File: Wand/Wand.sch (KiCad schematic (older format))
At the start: 20 parts, among them IC1 ATMEGA328P-A, J1 TIP, P1 ISP, P2 BASE, U1 OPA336U, U2 MPU-6050, Y1 16MHz

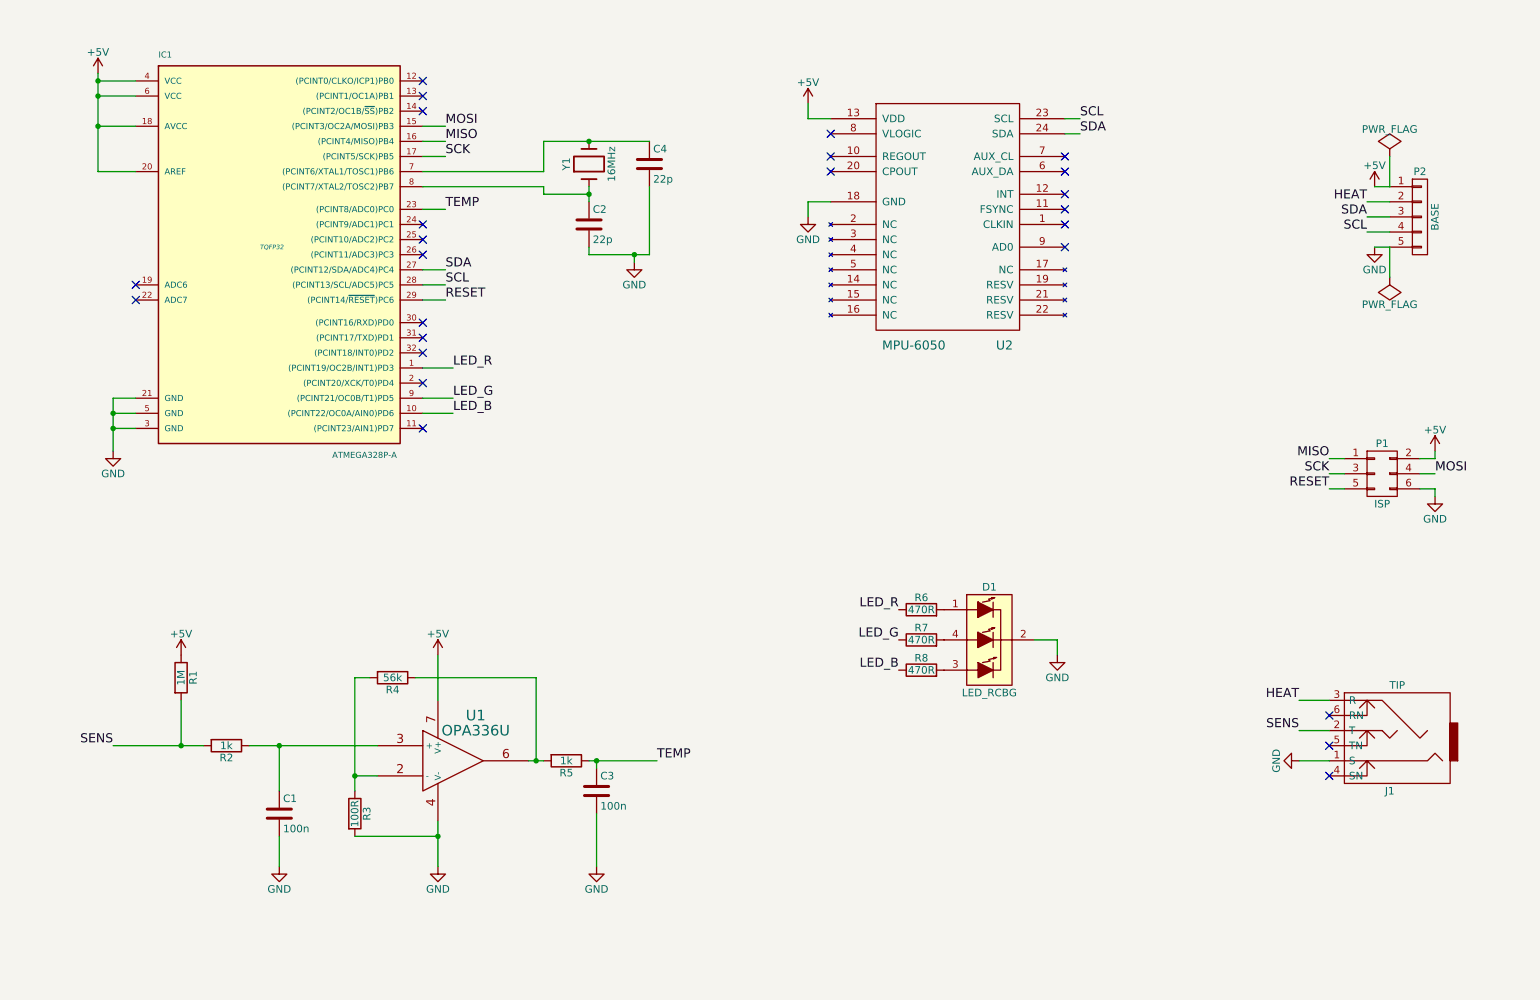
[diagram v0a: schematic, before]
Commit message: Changed logic voltage to 3.3V as the MCP-6050 is 3,3v (as are most accelerometers)
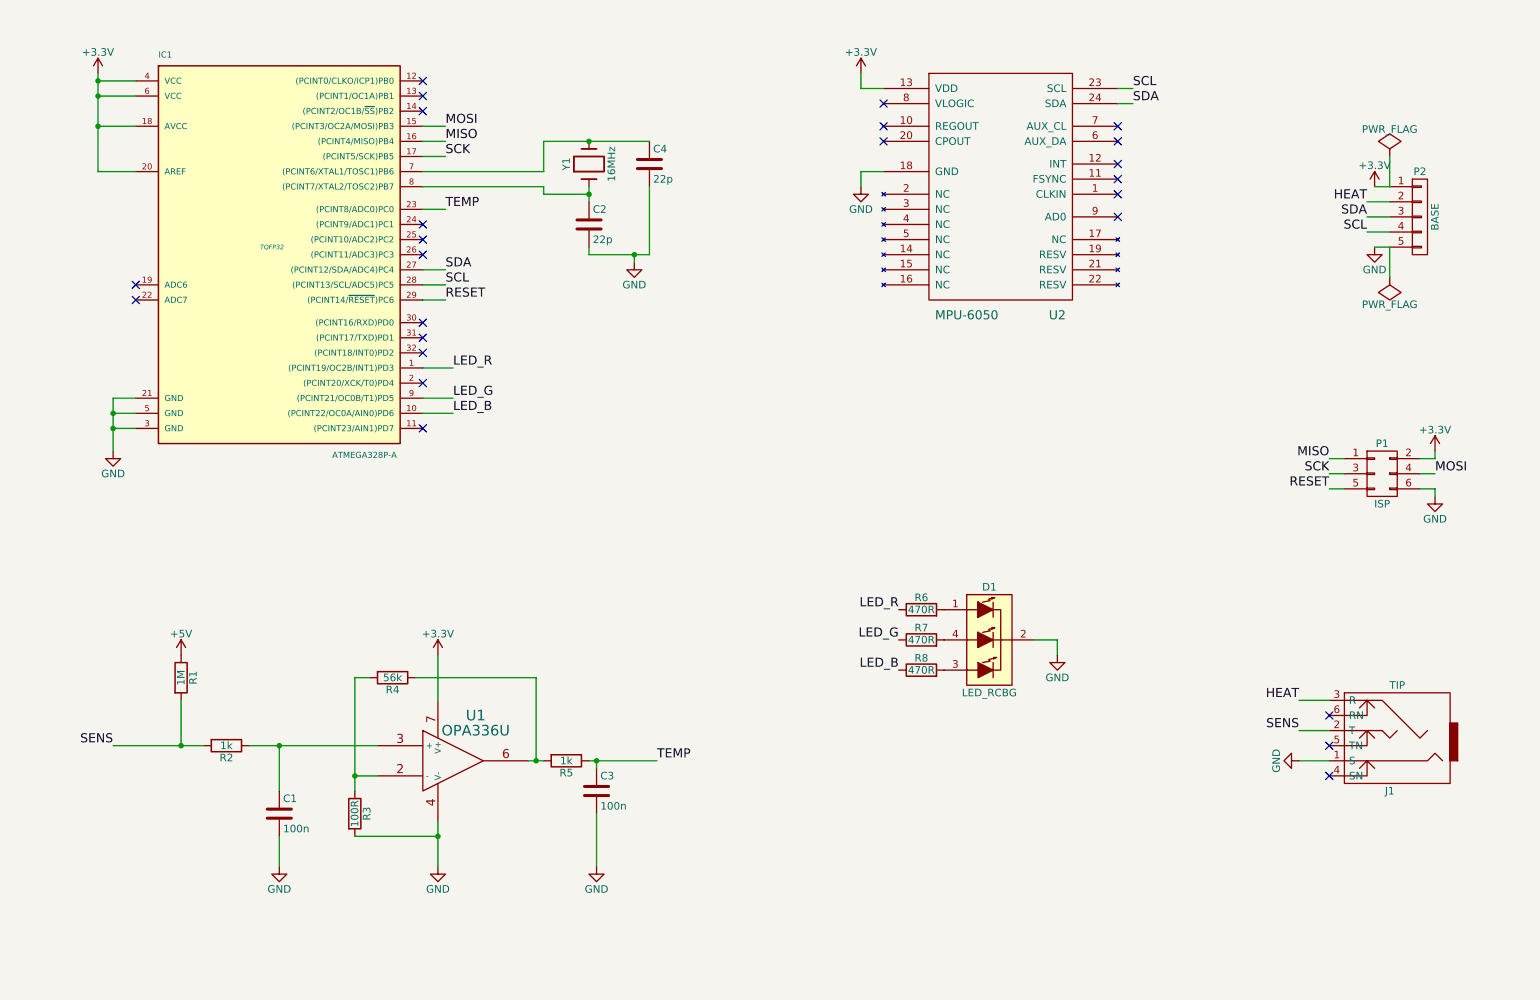
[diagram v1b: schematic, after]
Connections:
- net +5V: no longer IC1.18 (AVCC), IC1.20 (AREF), IC1.4 (VCC), IC1.6 (VCC), P1.2 (P2), P2.1 (P1), U1.7 (V+), U2.13 (VDD)
- new net +3V3: IC1.18 (AVCC), IC1.20 (AREF), IC1.4 (VCC), IC1.6 (VCC), P1.2 (P2), P2.1 (P1), U1.7 (V+), U2.13 (VDD)
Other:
- moved on the sheet: U2
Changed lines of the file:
@@
 LIBS:valves
 LIBS:mpu-6050
+LIBS:Wand
 LIBS:Wand-cache
 EELAYER 25 0
@@
 L MPU-6050 U2
 U 1 1 56411594
-P 7100 2300
-F 0 "U2" H 7450 1600 60  0000 C CNN
-F 1 "MPU-6050" H 6850 1600 60  0000 C CNN
-F 2 "" H 7100 2050 60  0000 C CNN
-F 3 "" H 7100 2050 60  0000 C CNN
-	1    7100 2300
+P 7450 2100
+F 0 "U2" H 7800 1400 60  0000 C CNN
+F 1 "MPU-6050" H 7200 1400 60  0000 C CNN
+F 2 "" H 7450 1850 60  0000 C CNN
+F 3 "" H 7450 1850 60  0000 C CNN
+	1    7450 2100
 	1    0    0    -1
 $EndComp
@@
 $EndComp
 $Comp
-L +5V #PWR01
-U 1 1 564124F5
-P 3700 5050
-F 0 "#PWR01" H 3700 4900 50  0001 C CNN
-F 1 "+5V" H 3700 5190 50  0000 C CNN
-F 2 "" H 3700 5050 60  0000 C CNN
-F 3 "" H 3700 5050 60  0000 C CNN
-	1    3700 5050
-	1    0    0    -1
-$EndComp
-$Comp
 L GND #PWR02
 U 1 1 5641252D
@@
 F 3 "" H 5000 2450 60  0000 C CNN
 	1    5000 2450
-	1    0    0    -1
-$EndComp
-$Comp
-L +5V #PWR08
-U 1 1 56415353
-P 1450 1200
-F 0 "#PWR08" H 1450 1050 50  0001 C CNN
-F 1 "+5V" H 1450 1340 50  0000 C CNN
-F 2 "" H 1450 1200 60  0000 C CNN
-F 3 "" H 1450 1200 60  0000 C CNN
-	1    1450 1200
 	1    0    0    -1
 $EndComp
@@
 Text Label 9600 3950 2    60   ~ 0
 RESET
-$Comp
-L +5V #PWR011
-U 1 1 56417CD8
-P 10300 3700
-F 0 "#PWR011" H 10300 3550 50  0001 C CNN
-F 1 "+5V" H 10300 3840 50  0000 C CNN
-F 2 "" H 10300 3700 60  0000 C CNN
-F 3 "" H 10300 3700 60  0000 C CNN
-	1    10300 3700
-	1    0    0    -1
-$EndComp
 Text Label 10300 3850 0    60   ~ 0
 MOSI
@@
 	1    0    0    -1
 $EndComp
-$Comp
-L +5V #PWR014
-U 1 1 56418042
-P 9900 1950
-F 0 "#PWR014" H 9900 1800 50  0001 C CNN
-F 1 "+5V" H 9900 2090 50  0000 C CNN
-F 2 "" H 9900 1950 60  0000 C CNN
-F 3 "" H 9900 1950 60  0000 C CNN
-	1    9900 1950
-	1    0    0    -1
-$EndComp
 Text Label 9850 2050 2    60   ~ 0
 HEAT
@@
 SCL
 Wire Wire Line
-	1550 5650 2150 5650
+	1550 5650 2000 5650
+Wire Wire Line
+	2000 5650 2150 5650
 Wire Wire Line
 	2000 5350 2000 5650
 Connection ~ 2000 5650
 Wire Wire Line
-	2450 5650 3300 5650
+	2450 5650 2650 5650
+Wire Wire Line
+	2650 5650 3300 5650
 Wire Wire Line
 	2650 5950 2650 5650
@@
 	2650 6250 2650 6450
 Wire Wire Line
-	3150 5200 3150 5950
+	3150 5200 3150 5850
+Wire Wire Line
+	3150 5850 3150 5950
 Wire Wire Line
 	3150 5850 3300 5850
@@
 	4350 5200 4350 5750
 Wire Wire Line
-	4300 5750 4400 5750
+	4300 5750 4350 5750
+Wire Wire Line
+	4350 5750 4400 5750
 Connection ~ 4350 5750
 Wire Wire Line
@@
 	3150 6250 3700 6250
 Wire Wire Line
-	3700 6150 3700 6450
+	3700 6150 3700 6250
+Wire Wire Line
+	3700 6250 3700 6450
 Connection ~ 3700 6250
 Wire Wire Line
 	4750 6100 4750 6450
 Wire Wire Line
-	4700 5750 5150 5750
+	4700 5750 4750 5750
+Wire Wire Line
+	4750 5750 5150 5750
 Wire Wire Line
 	4750 5750 4750 5800
@@
 	4400 1850 4400 1650
 Wire Wire Line
-	4400 1650 5100 1650
-Wire Wire Line
-	4700 1950 4700 2050
+	4400 1650 4700 1650
+Wire Wire Line
+	4700 1650 5100 1650
+Wire Wire Line
+	4700 1950 4700 2000
+Wire Wire Line
+	4700 2000 4700 2050
 Connection ~ 4700 1650
 Wire Wire Line
@@
 	5100 2400 5100 1950
 Wire Wire Line
-	4700 2400 5100 2400
+	4700 2400 5000 2400
+Wire Wire Line
+	5000 2400 5100 2400
 Wire Wire Line
 	5000 2400 5000 2450
@@
 Connection ~ 5000 2400
 Wire Wire Line
-	1450 1200 1450 1850
+	1450 1200 1450 1250
+Wire Wire Line
+	1450 1250 1450 1350
+Wire Wire Line
+	1450 1350 1450 1550
+Wire Wire Line
+	1450 1550 1450 1850
 Wire Wire Line
 	1450 1250 1700 1250
@@
 Connection ~ 1450 1250
 Wire Wire Line
-	1550 3350 1550 3700
+	1550 3350 1550 3450
+Wire Wire Line
+	1550 3450 1550 3550
+Wire Wire Line
+	1550 3550 1550 3700
 Wire Wire Line
 	1550 3550 1700 3550
@@
 Wire Wire Line
 	9900 2350 10000 2350
-Text Label 7950 1600 0    60   ~ 0
+Text Label 8300 1400 0    60   ~ 0
 SDA
-Text Label 7950 1500 0    60   ~ 0
+Text Label 8300 1300 0    60   ~ 0
 SCL
 Wire Wire Line
-	7950 1500 7850 1500
-Wire Wire Line
-	7850 1600 7950 1600
-$Comp
-L +5V #PWR015
-U 1 1 56419539
-P 6150 1400
-F 0 "#PWR015" H 6150 1250 50  0001 C CNN
-F 1 "+5V" H 6150 1540 50  0000 C CNN
-F 2 "" H 6150 1400 60  0000 C CNN
-F 3 "" H 6150 1400 60  0000 C CNN
-	1    6150 1400
-	1    0    0    -1
-$EndComp
+	8300 1300 8200 1300
+Wire Wire Line
+	8200 1400 8300 1400
 $Comp
 L GND #PWR016
 U 1 1 56419575
-P 6150 2150
-F 0 "#PWR016" H 6150 1900 50  0001 C CNN
-F 1 "GND" H 6150 2000 50  0000 C CNN
-F 2 "" H 6150 2150 60  0000 C CNN
-F 3 "" H 6150 2150 60  0000 C CNN
-	1    6150 2150
-	1    0    0    -1
-$EndComp
-Wire Wire Line
-	6150 2050 6150 2150
-Wire Wire Line
-	6150 2050 6300 2050
-Wire Wire Line
-	6300 1500 6150 1500
-Wire Wire Line
-	6150 1500 6150 1400
+P 6500 1950
+F 0 "#PWR016" H 6500 1700 50  0001 C CNN
+F 1 "GND" H 6500 1800 50  0000 C CNN
+F 2 "" H 6500 1950 60  0000 C CNN
+F 3 "" H 6500 1950 60  0000 C CNN
+	1    6500 1950
+	1    0    0    -1
+$EndComp
+Wire Wire Line
+	6500 1850 6500 1950
+Wire Wire Line
+	6500 1850 6650 1850
+Wire Wire Line
+	6650 1300 6500 1300
+Wire Wire Line
+	6500 1300 6500 1200
 Text Label 3750 2500 0    60   ~ 0
 SDA
@@
 NoConn ~ 3600 1350
 NoConn ~ 3600 1250
-NoConn ~ 6300 1600
-NoConn ~ 6300 1750
-NoConn ~ 6300 1850
-NoConn ~ 7850 2350
-NoConn ~ 7850 2200
-NoConn ~ 7850 2100
-NoConn ~ 7850 2000
-NoConn ~ 7850 1850
-NoConn ~ 7850 1750
+NoConn ~ 6650 1400
+NoConn ~ 6650 1550
+NoConn ~ 6650 1650
+NoConn ~ 8200 2150
+NoConn ~ 8200 2000
+NoConn ~ 8200 1900
+NoConn ~ 8200 1800
+NoConn ~ 8200 1650
+NoConn ~ 8200 1550
 $Comp
 L PWR_FLAG #FLG017
@@
 Wire Wire Line
 	10300 3950 10300 4000
+$Comp
+L +3.3V #PWR?
+U 1 1 5647AD9A
+P 9900 1950
+F 0 "#PWR?" H 9900 1800 50  0001 C CNN
+F 1 "+3.3V" H 9900 2090 50  0000 C CNN
+F 2 "" H 9900 1950 60  0000 C CNN
+F 3 "" H 9900 1950 60  0000 C CNN
+	1    9900 1950
+	1    0    0    -1
+$EndComp
+$Comp
+L +3.3V #PWR?
+U 1 1 5647B486
+P 6500 1200
+F 0 "#PWR?" H 6500 1050 50  0001 C CNN
+F 1 "+3.3V" H 6500 1340 50  0000 C CNN
+F 2 "" H 6500 1200 60  0000 C CNN
+F 3 "" H 6500 1200 60  0000 C CNN
+	1    6500 1200
+	1    0    0    -1
+$EndComp
+$Comp
+L +3.3V #PWR?
+U 1 1 5647BAD5
+P 1450 1200
+F 0 "#PWR?" H 1450 1050 50  0001 C CNN
+F 1 "+3.3V" H 1450 1340 50  0000 C CNN
+F 2 "" H 1450 1200 60  0000 C CNN
+F 3 "" H 1450 1200 60  0000 C CNN
+	1    1450 1200
+	1    0    0    -1
+$EndComp
+$Comp
+L +3.3V #PWR?
+U 1 1 5647C7BA
+P 3700 5050
+F 0 "#PWR?" H 3700 4900 50  0001 C CNN
+F 1 "+3.3V" H 3700 5190 50  0000 C CNN
+F 2 "" H 3700 5050 60  0000 C CNN
+F 3 "" H 3700 5050 60  0000 C CNN
+	1    3700 5050
+	1    0    0    -1
+$EndComp
+$Comp
+L +3.3V #PWR?
+U 1 1 5647DBFE
+P 10300 3700
+F 0 "#PWR?" H 10300 3550 50  0001 C CNN
+F 1 "+3.3V" H 10300 3840 50  0000 C CNN
+F 2 "" H 10300 3700 60  0000 C CNN
+F 3 "" H 10300 3700 60  0000 C CNN
+	1    10300 3700
+	1    0    0    -1
+$EndComp
 $EndSCHEMATC

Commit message: Use UART to communicate with the base unit, should be more reliable than I2C over long (1-2m).
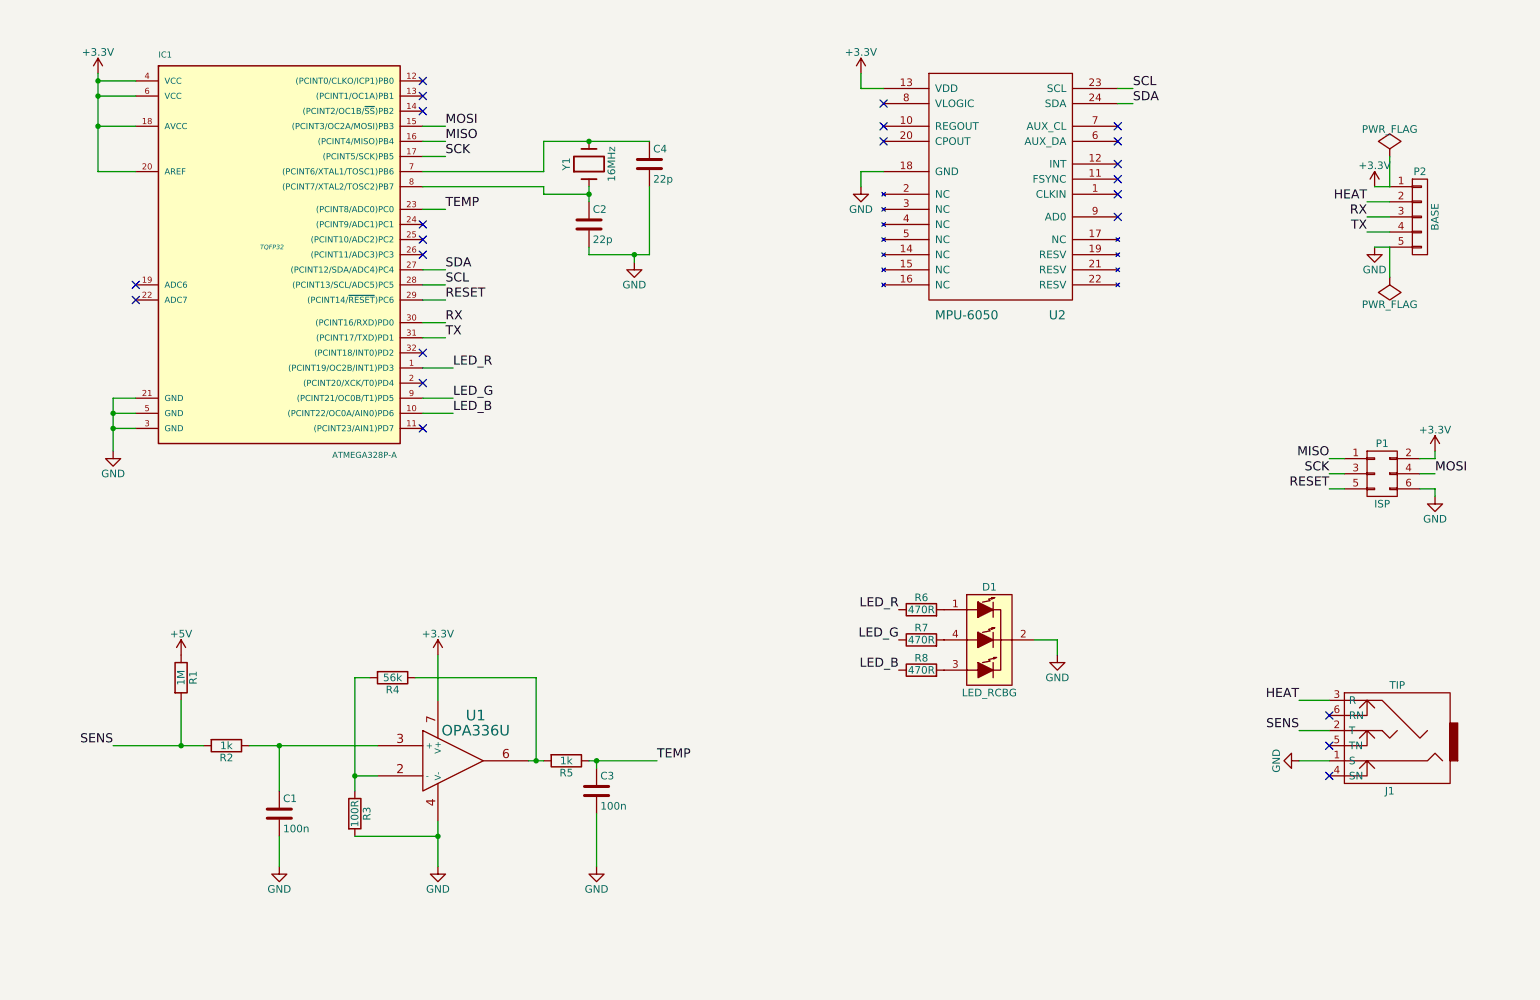
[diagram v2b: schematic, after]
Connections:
- net SCL: no longer P2.4 (P4)
- net SDA: no longer P2.3 (P3)
- net RX: now reaches IC1.30 ((PCINT16/RXD)PD0)
- net RX: now also P2.3 (P3)
- net TX: now reaches IC1.31 ((PCINT17/TXD)PD1)
- net TX: now also P2.4 (P4)
- no-connect marks 25 -> 23
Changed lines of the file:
@@
 Text Label 9850 2050 2    60   ~ 0
 HEAT
-Text Label 9850 2150 2    60   ~ 0
-SDA
-Text Label 9850 2250 2    60   ~ 0
-SCL
-Wire Wire Line
-	1550 5650 2000 5650
-Wire Wire Line
-	2000 5650 2150 5650
+Wire Wire Line
+	1550 5650 2150 5650
 Wire Wire Line
 	2000 5350 2000 5650
 Connection ~ 2000 5650
 Wire Wire Line
-	2450 5650 2650 5650
-Wire Wire Line
-	2650 5650 3300 5650
+	2450 5650 3300 5650
 Wire Wire Line
 	2650 5950 2650 5650
@@
 	2650 6250 2650 6450
 Wire Wire Line
-	3150 5200 3150 5850
-Wire Wire Line
-	3150 5850 3150 5950
+	3150 5200 3150 5950
 Wire Wire Line
 	3150 5850 3300 5850
@@
 	4350 5200 4350 5750
 Wire Wire Line
-	4300 5750 4350 5750
-Wire Wire Line
-	4350 5750 4400 5750
+	4300 5750 4400 5750
 Connection ~ 4350 5750
 Wire Wire Line
@@
 	3150 6250 3700 6250
 Wire Wire Line
-	3700 6150 3700 6250
-Wire Wire Line
-	3700 6250 3700 6450
+	3700 6150 3700 6450
 Connection ~ 3700 6250
 Wire Wire Line
 	4750 6100 4750 6450
 Wire Wire Line
-	4700 5750 4750 5750
-Wire Wire Line
-	4750 5750 5150 5750
+	4700 5750 5150 5750
 Wire Wire Line
 	4750 5750 4750 5800
@@
 	4400 1850 4400 1650
 Wire Wire Line
-	4400 1650 4700 1650
-Wire Wire Line
-	4700 1650 5100 1650
-Wire Wire Line
-	4700 1950 4700 2000
-Wire Wire Line
-	4700 2000 4700 2050
+	4400 1650 5100 1650
+Wire Wire Line
+	4700 1950 4700 2050
 Connection ~ 4700 1650
 Wire Wire Line
@@
 	5100 2400 5100 1950
 Wire Wire Line
-	4700 2400 5000 2400
-Wire Wire Line
-	5000 2400 5100 2400
+	4700 2400 5100 2400
 Wire Wire Line
 	5000 2400 5000 2450
@@
 Connection ~ 5000 2400
 Wire Wire Line
-	1450 1200 1450 1250
-Wire Wire Line
-	1450 1250 1450 1350
-Wire Wire Line
-	1450 1350 1450 1550
-Wire Wire Line
-	1450 1550 1450 1850
+	1450 1200 1450 1850
 Wire Wire Line
 	1450 1250 1700 1250
@@
 Connection ~ 1450 1250
 Wire Wire Line
-	1550 3350 1550 3450
-Wire Wire Line
-	1550 3450 1550 3550
-Wire Wire Line
-	1550 3550 1550 3700
+	1550 3350 1550 3700
 Wire Wire Line
 	1550 3550 1700 3550
@@
 NoConn ~ 3600 3250
 NoConn ~ 3600 3050
-NoConn ~ 3600 2950
-NoConn ~ 3600 2850
 NoConn ~ 3600 2400
 NoConn ~ 3600 2300
@@
 	1    0    0    -1
 $EndComp
+Text Label 3750 2850 0    60   ~ 0
+RX
+Text Label 3750 2950 0    60   ~ 0
+TX
+Wire Wire Line
+	3600 2850 3750 2850
+Wire Wire Line
+	3600 2950 3750 2950
+Text Label 9850 2250 2    60   ~ 0
+TX
+Text Label 9850 2150 2    60   ~ 0
+RX
 $EndSCHEMATC
